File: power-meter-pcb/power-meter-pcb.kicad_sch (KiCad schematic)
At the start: 25 parts, among them J1 Crank interconnect, J2 Debug, J3 Spare GPIO pins, SW1 EN, SW2 BOOT, U1 ESP32-S3-MINI-1, U2 P3T1755

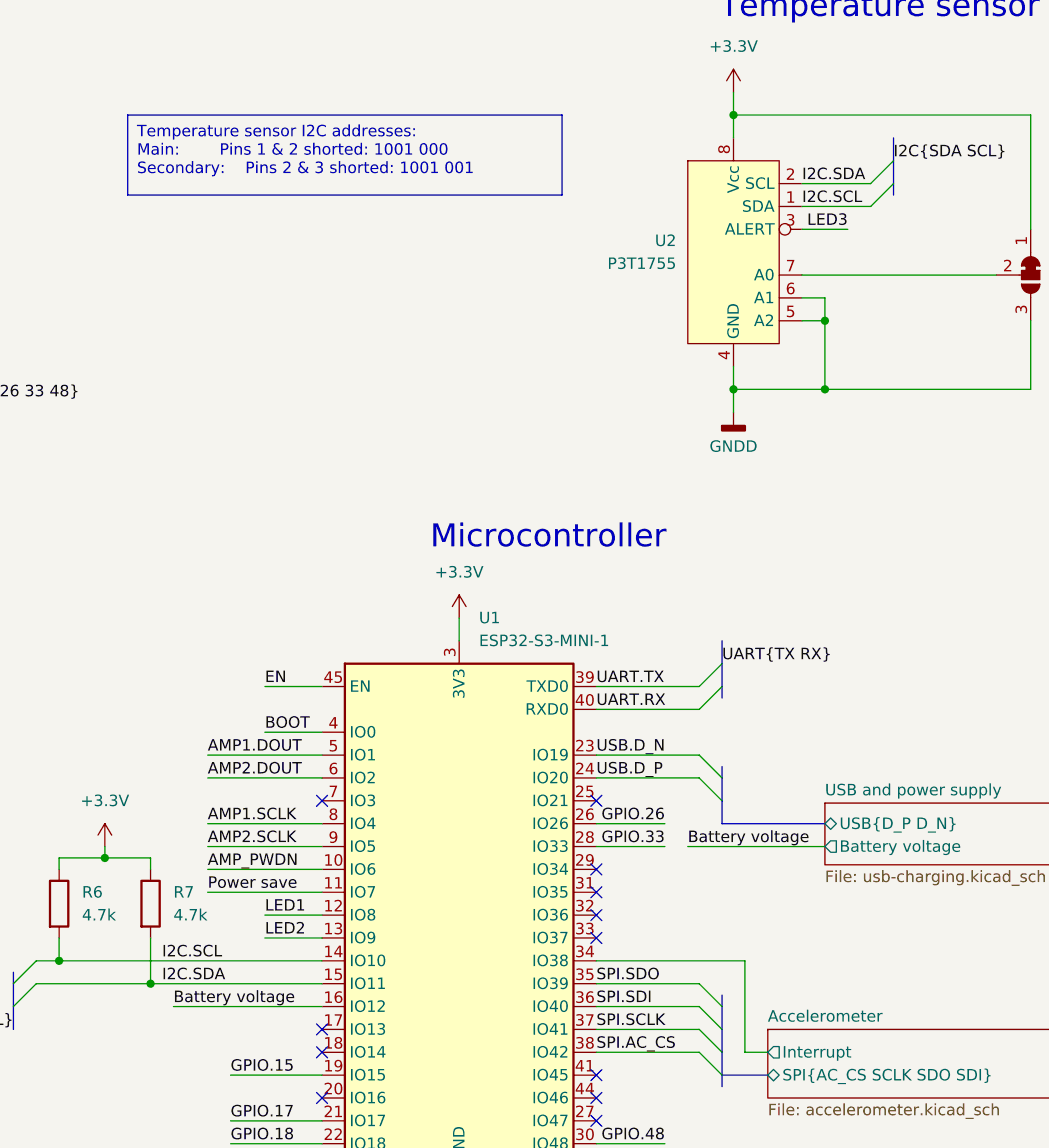
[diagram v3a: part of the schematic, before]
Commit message: Reads temperature, flashes amber LED, corrected bus labelling error in schematic.
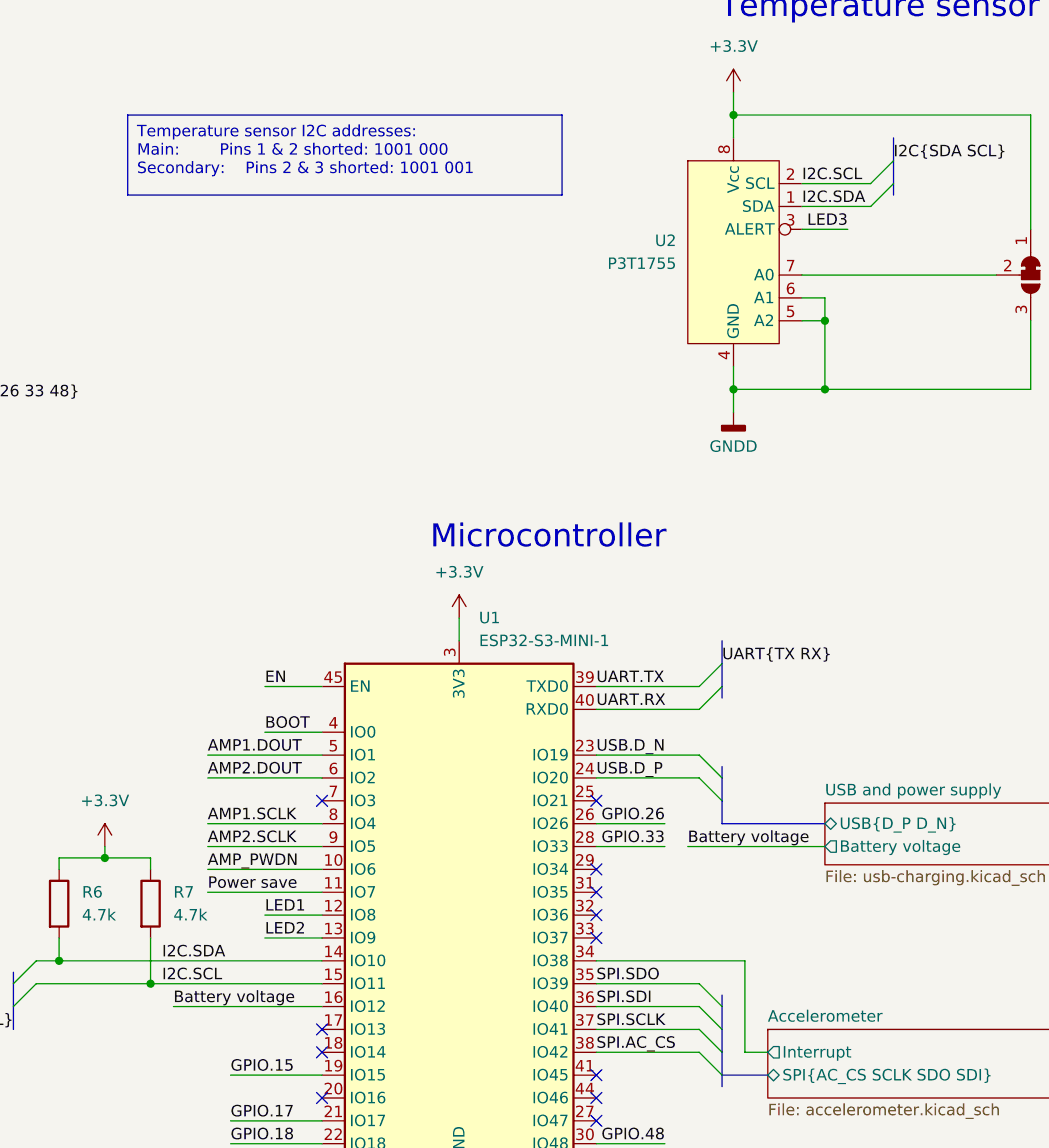
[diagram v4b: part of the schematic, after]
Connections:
- net I2C.SCL: now also R7.2, U1.15 (IO11), U2.2 (SCL); no longer R6.2, U1.14 (IO10), U2.1 (SDA)
- net I2C.SDA: now also R6.2, U1.14 (IO10), U2.1 (SDA); no longer R7.2, U1.15 (IO11), U2.2 (SCL)
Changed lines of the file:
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@@
 		)
 	)
-	(label "I2C.SDA"
+	(label "I2C.SCL"
 		(at 166.37 130.81 0)
 		(fields_autoplaced yes)
@@
 		)
 	)
-	(label "I2C.SCL"
+	(label "I2C.SDA"
 		(at 237.49 44.45 0)
 		(fields_autoplaced yes)
@@
 		)
 	)
-	(label "I2C.SCL"
+	(label "I2C.SDA"
 		(at 166.37 128.27 0)
 		(fields_autoplaced yes)
@@
 		)
 	)
-	(label "I2C.SDA"
+	(label "I2C.SCL"
 		(at 237.49 41.91 0)
 		(fields_autoplaced yes)

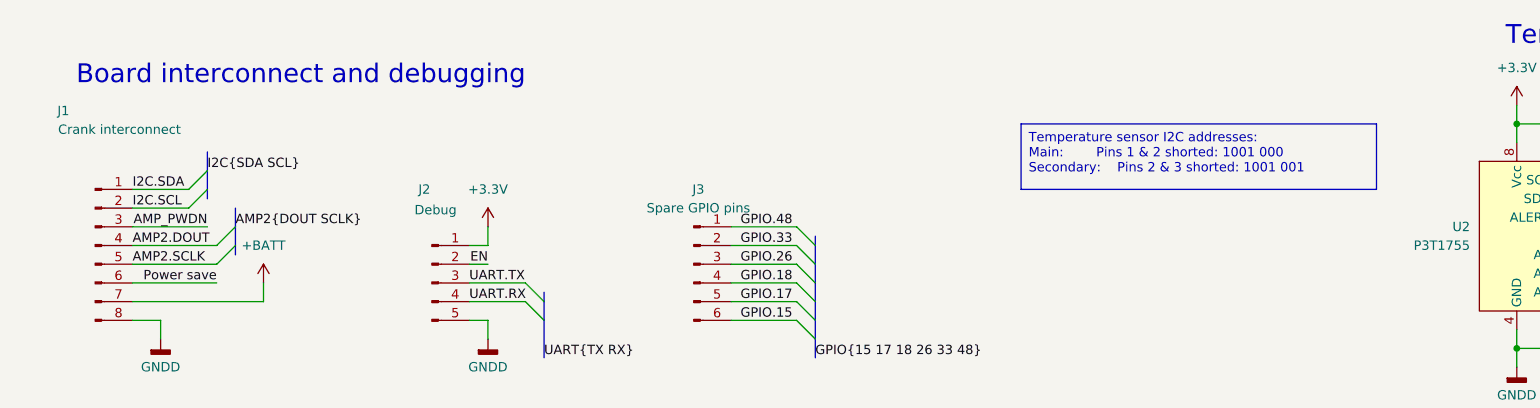
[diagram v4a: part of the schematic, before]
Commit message: Fixing I2C track labelling. V1.1.0
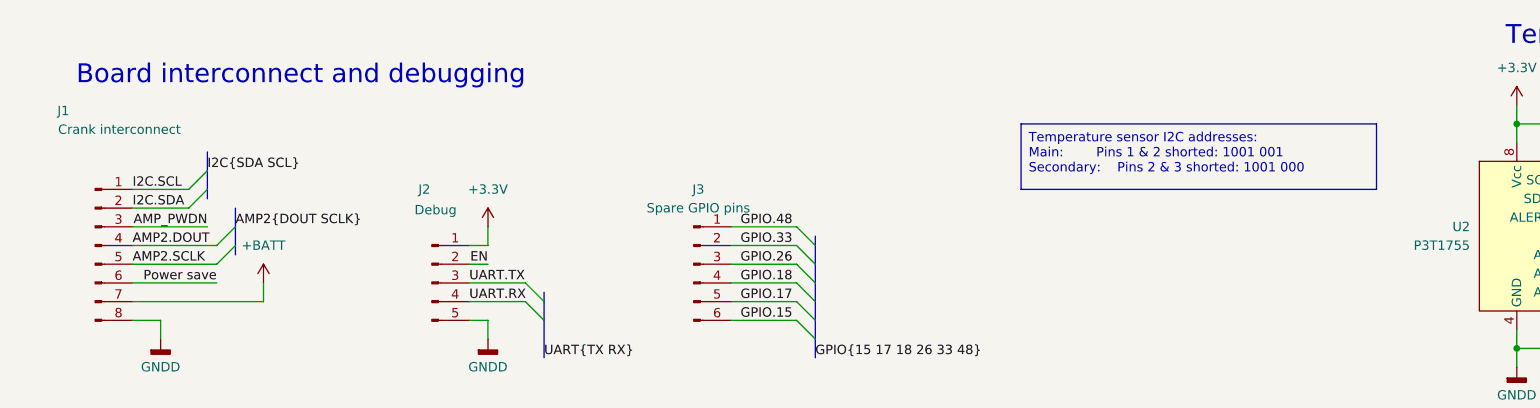
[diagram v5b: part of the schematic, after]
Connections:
- net I2C.SCL: now also J1.1 (Pin_1); no longer J1.2 (Pin_2)
- net I2C.SDA: now also J1.2 (Pin_2); no longer J1.1 (Pin_1)
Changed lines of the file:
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@@
 	(title_block
 		(title "Cycling power meter FYP")
-		(date "2024-07-15")
-		(rev "V1.0.4")
+		(date "2024-08-08")
+		(rev "V1.1.0")
 		(company "Monash Human Power - Jotham Gates & Oscar Varney")
 		(comment 1 "For the secondary crank, set J3 to short pins 2 and 3 and short J1 and J2.")
@@
 		)
 	)
-	(text_box "Temperature sensor I2C addresses:\nMain:		Pins 1 & 2 shorted: 1001 000\nSecondary:	Pins 2 & 3 shorted: 1001 001"
+	(text_box "Temperature sensor I2C addresses:\nMain:		Pins 1 & 2 shorted: 1001 001\nSecondary:	Pins 2 & 3 shorted: 1001 000"
 		(exclude_from_sim no)
 		(at 162.56 34.29 0)
@@
 		)
 	)
-	(label "I2C.SCL"
+	(label "I2C.SDA"
 		(at 41.91 45.72 0)
 		(fields_autoplaced yes)
@@
 		)
 	)
-	(label "I2C.SDA"
+	(label "I2C.SCL"
 		(at 41.91 43.18 0)
 		(fields_autoplaced yes)

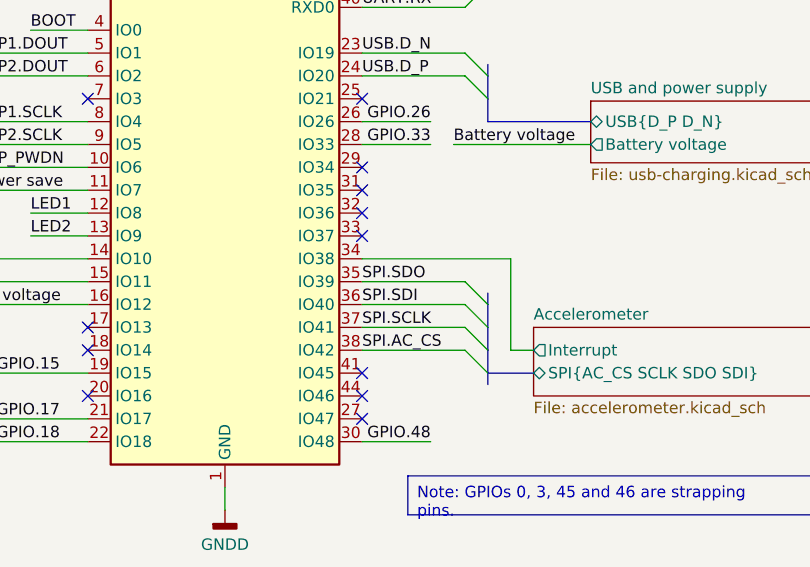
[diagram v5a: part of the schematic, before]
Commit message: Fixed SPI pin labels
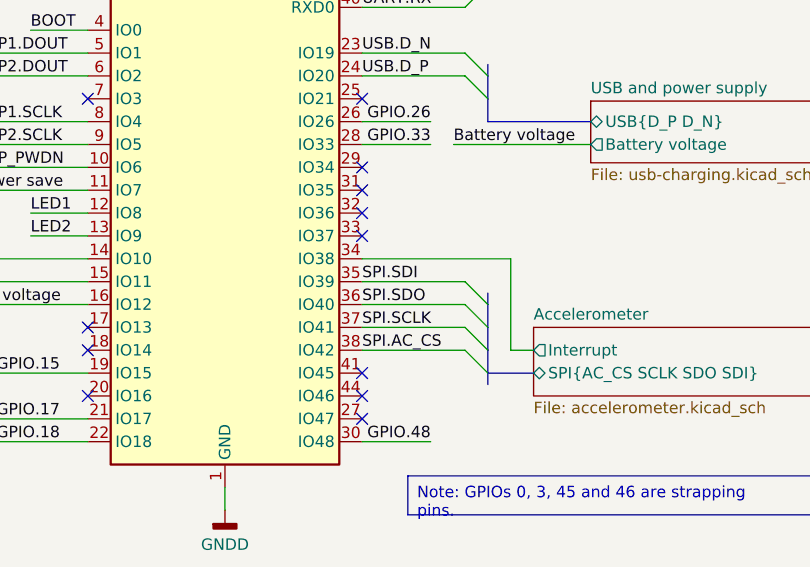
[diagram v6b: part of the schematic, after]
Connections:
- net SPI.SDI: now also U1.35 (IO39); no longer U1.36 (IO40)
- net SPI.SDO: now also U1.36 (IO40); no longer U1.35 (IO39)
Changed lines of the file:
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@@
 		)
 	)
-	(label "SPI.SDO"
+	(label "SPI.SDI"
 		(at 214.63 130.81 0)
 		(fields_autoplaced yes)
@@
 		)
 	)
-	(label "SPI.SDI"
+	(label "SPI.SDO"
 		(at 214.63 133.35 0)
 		(fields_autoplaced yes)

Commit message: PCB modifications about done
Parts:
- removed D1, D2: LED, LED_SMD:LED_0603_1608Metric_Pad1.05x0.95mm_HandSolder, symbol Device:LED
- added D1: CLX6F-FKC-CNP1ST1E1BB7D3D3, RGB_LED_CLX6F-FKC-CNP1ST1E1BB7D3D3:PLCC6_3.4X3.4_CRW-M, symbol RGB_LED_CLX6F-FKC-CNP1ST1E1BB7D3D3:CLX6F-FKC-CNP1ST1E1BB7D3D3
- added R19: 150, Resistor_SMD:R_0603_1608Metric_Pad0.98x0.95mm_HandSolder, symbol Device:R
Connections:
- net Accelerometer/Interrupt: now also U1.25 (IO21); no longer U1.34 (IO38)
- net Battery voltage: now also U1.17 (IO13); no longer U1.16 (IO12)
- net GNDD: now also D1.1, D1.2, D1.3
- net GPIO.17: now also J3.4 (Pin_4); no longer J3.5 (Pin_5)
- net GPIO.18: now also J3.3 (Pin_3); no longer J3.4 (Pin_4)
- net GPIO.16: now reaches U1.20 (IO16)
- net GPIO.16: now also J3.5 (Pin_5)
- net at R4.2: now also D1.5
- net at R3.2: now also D1.4
- net GPIO.26: no longer names the net of U1.26 (IO26)
- net GPIO.26: no longer J3.3 (Pin_3)
- net LED1 renamed LEDB
- net LEDB: now also R19.1; no longer R3.1
- net LED2 renamed LEDG
- new net: D1.6, R19.2
- new net LEDR: R3.1, U1.16 (IO12)
- no-connect marks 12 -> 11
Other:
- moved on the sheet: C1, C2, D3, H1, H2, H3, R1, R2, R3, R4, R5, R6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

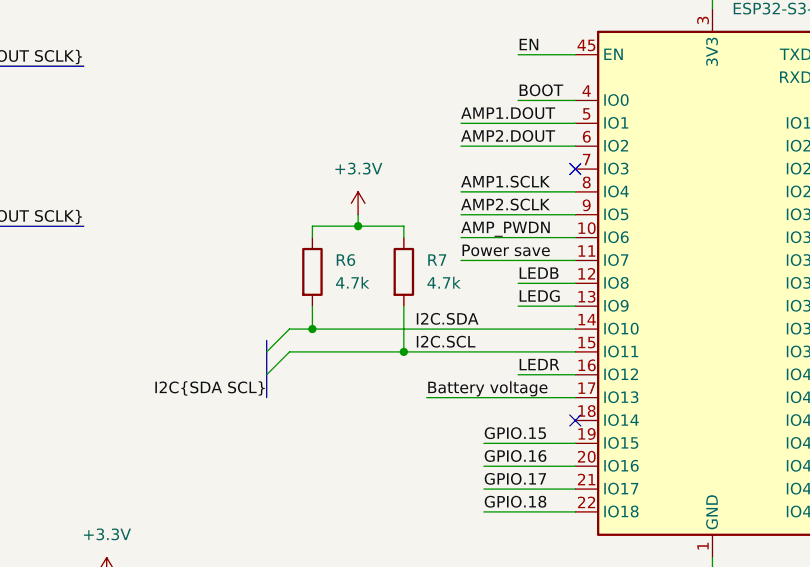
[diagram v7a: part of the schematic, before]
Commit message: Sorting out parts to order and component changes
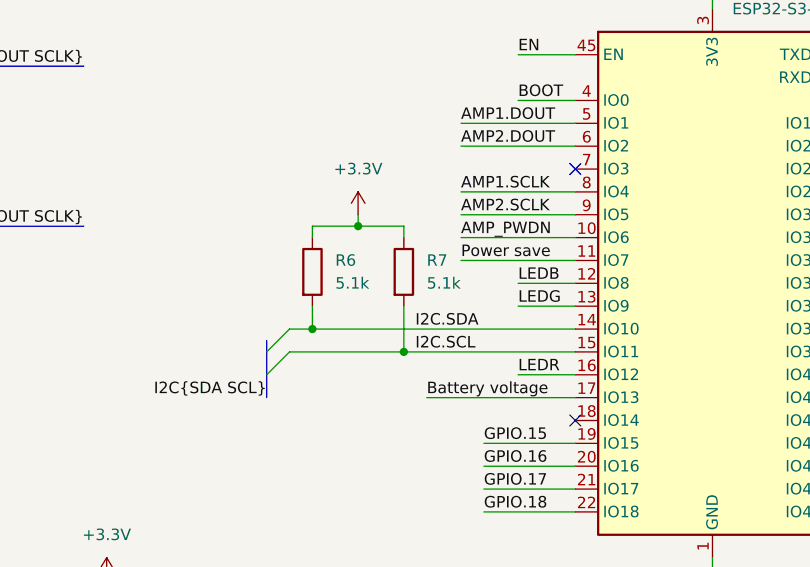
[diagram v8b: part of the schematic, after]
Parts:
- C1, C2, D3, H1, H2, H3, J1, J2, JP1, JP2, JP3, R1, R2, R3, R4, R5, SW1, SW2, U1, U2: SchematicVersionModified (none) -> V1.0.4
- D1: PlaceOnSecondary (none) -> No; SchematicVersionModified (none) -> V1.1.1
- J3: PlaceOnSecondary (none) -> No; SchematicVersionModified (none) -> V1.0.4
- R19: SchematicVersionModified (none) -> V1.1.1
- R6, R7: value 4.7k -> 5.1k; SchematicVersionModified (none) -> V1.1.1
